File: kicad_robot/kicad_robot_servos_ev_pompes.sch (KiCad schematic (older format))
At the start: 60 parts

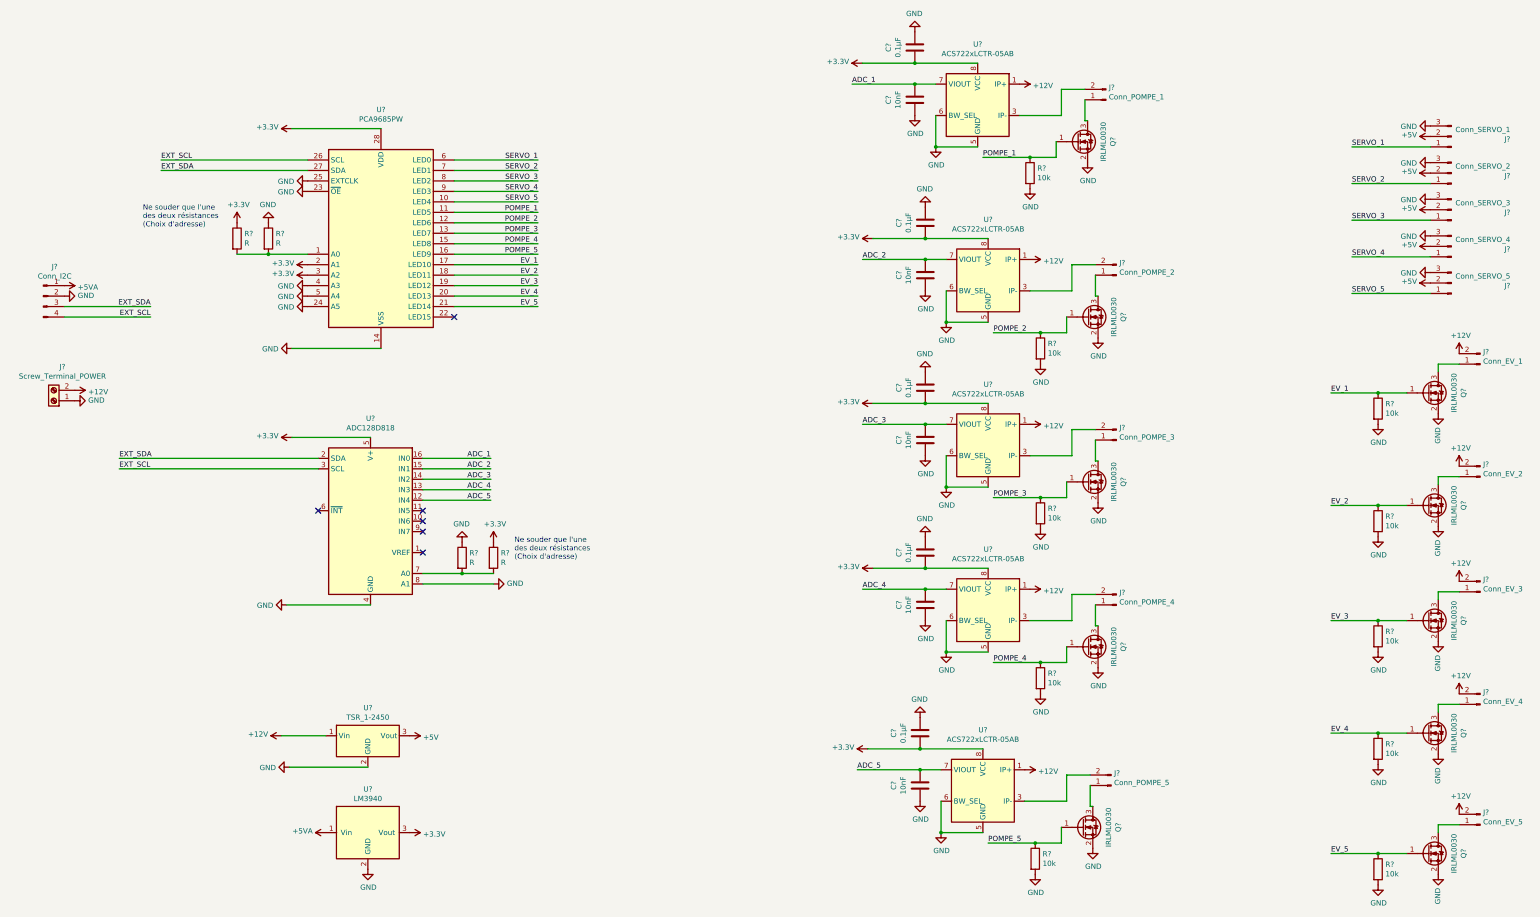
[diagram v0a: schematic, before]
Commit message: Reversed some connectors
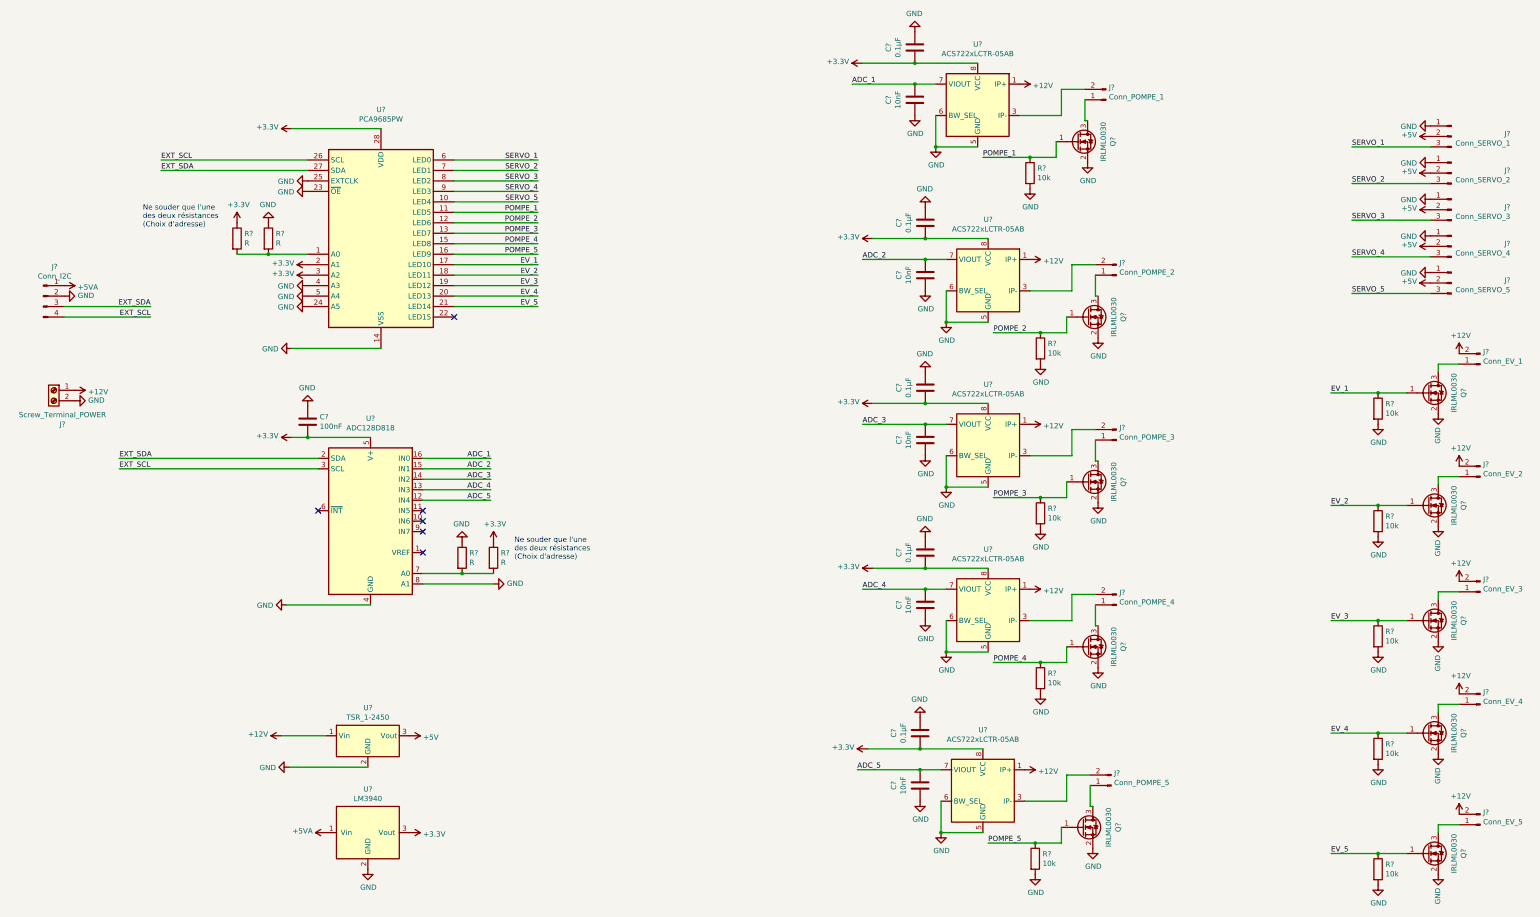
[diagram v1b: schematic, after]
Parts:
- added C?: 100nF, symbol Device:C
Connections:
- net +12V: now also J?.1 (Pin_1); no longer J?.2 (Pin_2)
- net +3V3: now also C?.2
- net GND: now also J?.1 (Pin_1), J?.1 (Pin_1), J?.1 (Pin_1), J?.1 (Pin_1), J?.1 (Pin_1), J?.2 (Pin_2), C?.1; no longer J?.1 (Pin_1), J?.3 (Pin_3), J?.3 (Pin_3), J?.3 (Pin_3), J?.3 (Pin_3), J?.3 (Pin_3)
- net SERVO_1: now also J?.3 (Pin_3); no longer J?.1 (Pin_1)
- net SERVO_2: now also J?.3 (Pin_3); no longer J?.1 (Pin_1)
- net SERVO_3: now also J?.3 (Pin_3); no longer J?.1 (Pin_1)
- net SERVO_4: now also J?.3 (Pin_3); no longer J?.1 (Pin_1)
- net SERVO_5: now also J?.3 (Pin_3); no longer J?.1 (Pin_1)

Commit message: Capa de découplage PCA
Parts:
- added C?: 100nF, symbol Device:C
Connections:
- net GND: now also C?.1
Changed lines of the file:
@@
+	-1   0    0    1
+$EndComp
+$Comp
+L Device:C C?
+U 1 1 60443C26
+P 3300 1700
+F 0 "C?" H 3415 1746 50  0000 L CNN
+F 1 "100nF" H 3415 1655 50  0000 L CNN
+F 2 "" H 3338 1550 50  0001 C CNN
+F 3 "~" H 3300 1700 50  0001 C CNN
+	1    3300 1700
+	1    0    0    -1
+$EndComp
+$Comp
+L power:GND #PWR?
+U 1 1 60443C2C
+P 3300 1550
+F 0 "#PWR?" H 3300 1300 50  0001 C CNN
+F 1 "GND" H 3305 1377 50  0000 C CNN
+F 2 "" H 3300 1550 50  0001 C CNN
+F 3 "" H 3300 1550 50  0001 C CNN
+	1    3300 1550
 	-1   0    0    1
 $EndComp

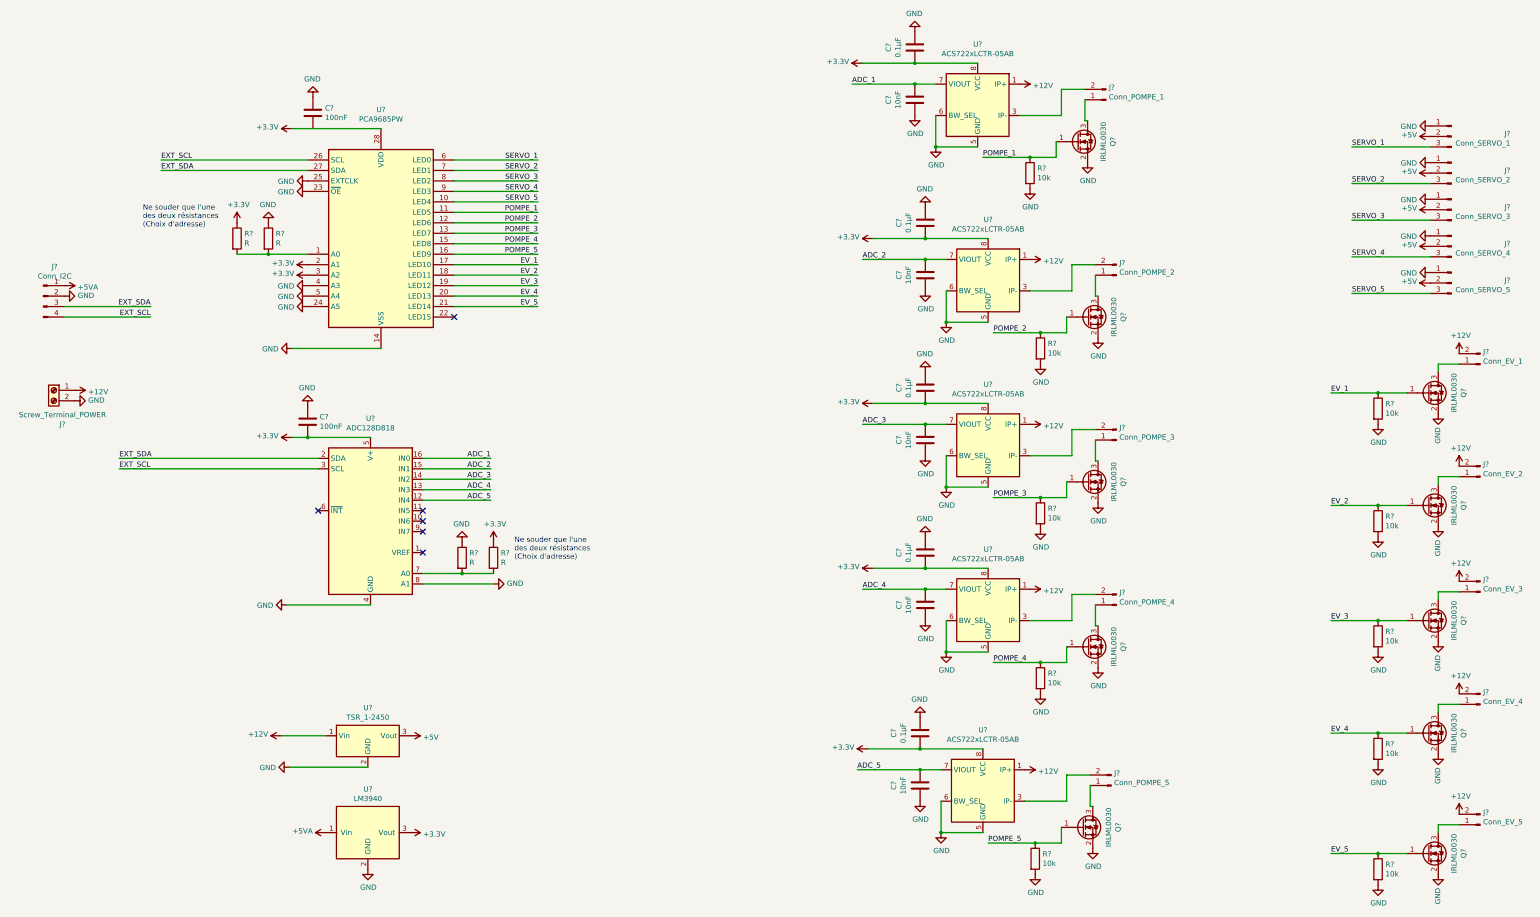
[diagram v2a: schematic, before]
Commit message: Footprint attribution
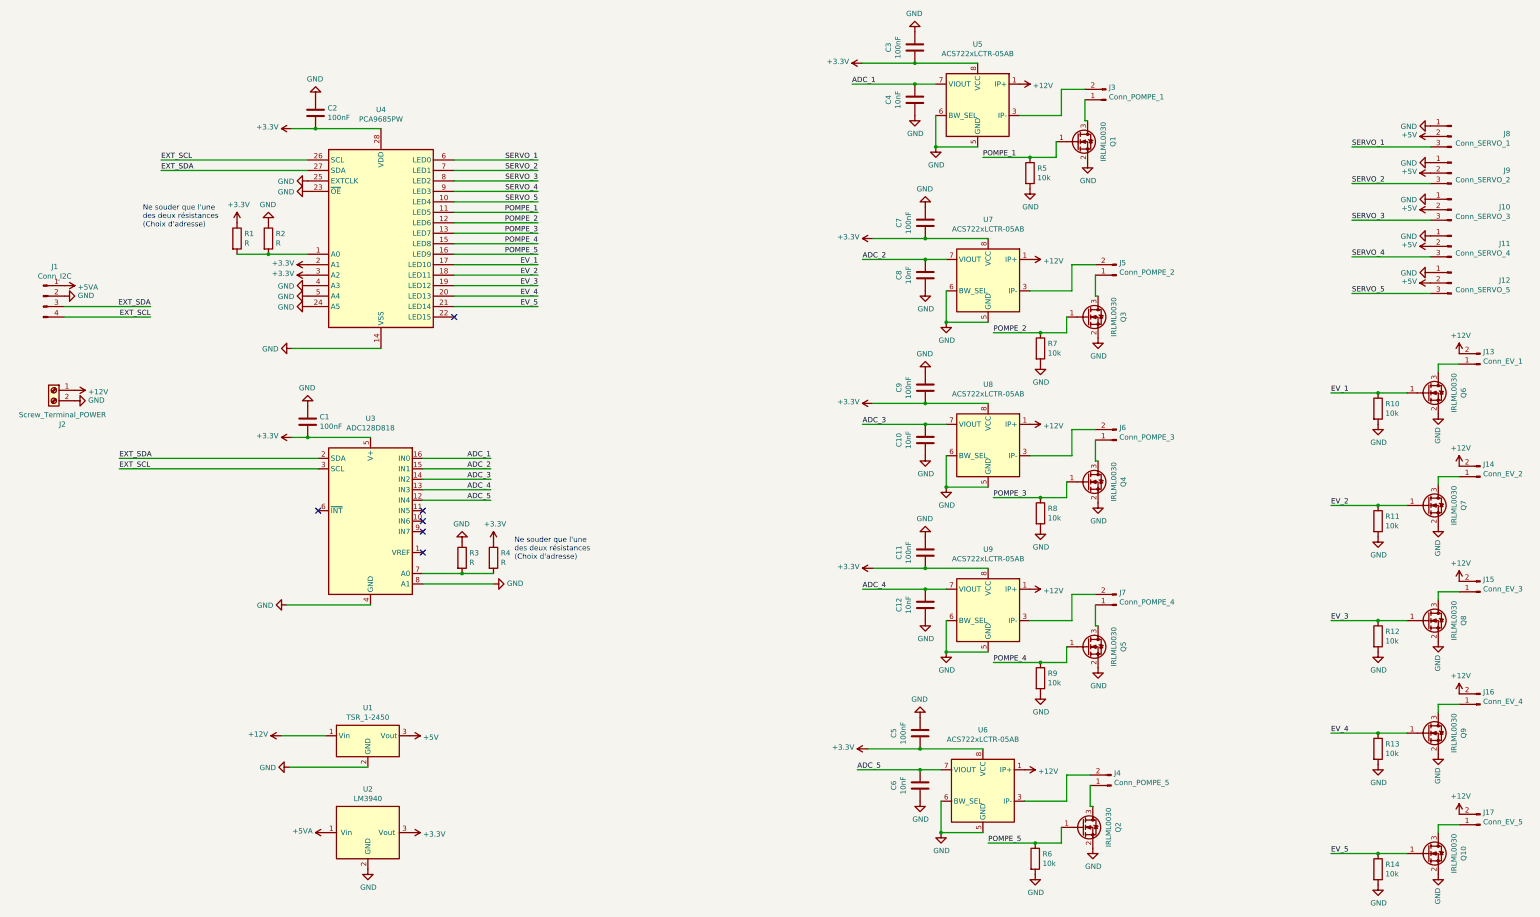
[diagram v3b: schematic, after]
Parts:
- C1, C10, C12, C2, C4, C6, C8: renamed from C?; footprint (none) -> Capacitor_SMD:C_0603_1608Metric_Pad1.08x0.95mm_HandSolder
- C11, C3, C5, C7, C9: renamed from C?; value 0.1µF -> 100nF; footprint (none) -> Capacitor_SMD:C_0603_1608Metric_Pad1.08x0.95mm_HandSolder
- J1: renamed from J?; footprint (none) -> Connector_JST:JST_XH_B4B-XH-A_1x04_P2.50mm_Vertical
- J10, J11, J12, J8, J9: renamed from J?; footprint (none) -> Connector_PinHeader_2.54mm:PinHeader_1x03_P2.54mm_Vertical
- J13, J14, J15, J16, J17, J3, J4, J5, J6, J7: renamed from J?; footprint (none) -> Connector_JST:JST_XH_B2B-XH-A_1x02_P2.50mm_Vertical
- J2: renamed from J?; footprint (none) -> TerminalBlock:TerminalBlock_bornier-2_P5.08mm
- R1, R10, R11, R12, R13, R14, R2, R3, R4, R5, R6, R7, R8, R9: renamed from R?; footprint (none) -> Resistor_SMD:R_0603_1608Metric_Pad0.98x0.95mm_HandSolder
- gave numbers to parts that had none: 19
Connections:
- net +3V3: now also C2.2
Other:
- moved on the sheet: C2
